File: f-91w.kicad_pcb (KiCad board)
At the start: 4 copper layers, 24.4 x 24.4 mm, 46 parts, among them P1 CONN_01X01, P10 CONN_01X01, P11 CONN_01X01, P13 CONN_01X01, P14 CONN_01X01, P2 CONN_01X01, P3 CONN_01X01, P5 CONN_01X01, P6 CONN_01X01, P7 CONN_01X01, P8 CONN_01X01, P9 CONN_01X01, Q1 BC846, U1 CY8C4248LQI-BL483, U2 LCD-F-91W, U3 BME680, Y1 32.768KHz, Y2 24MHz

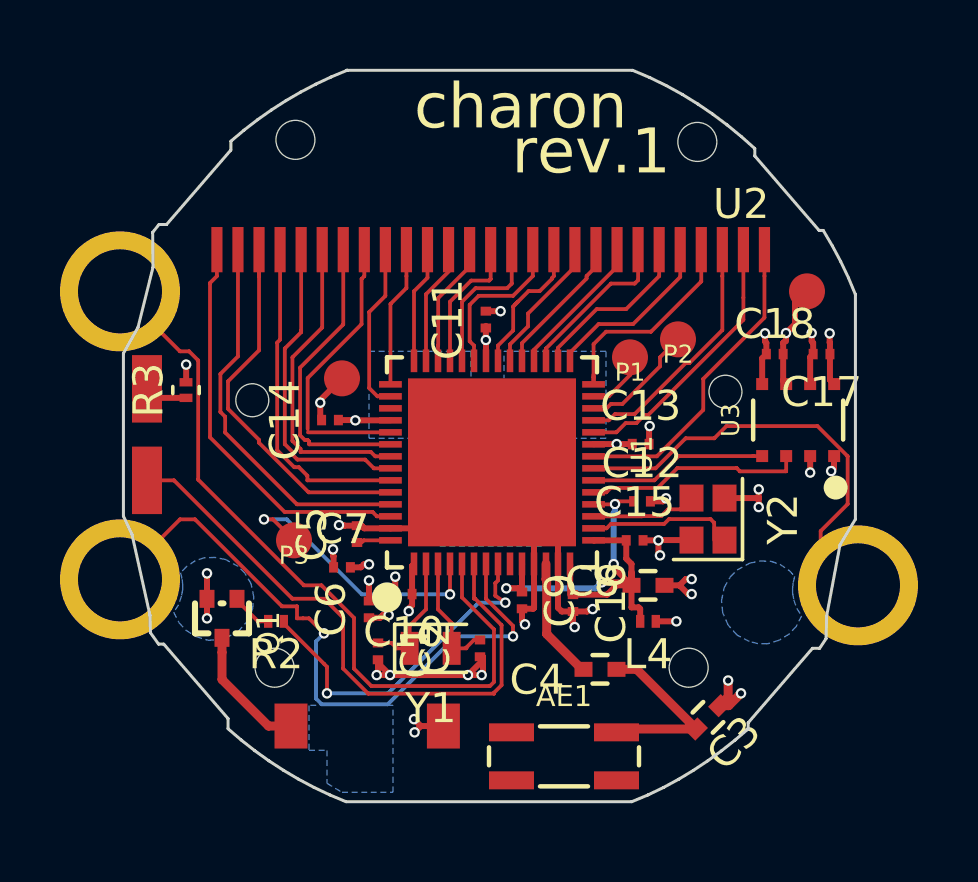
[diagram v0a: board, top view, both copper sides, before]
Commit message: Add outer ground planes, keepout and stitching vias for antenna
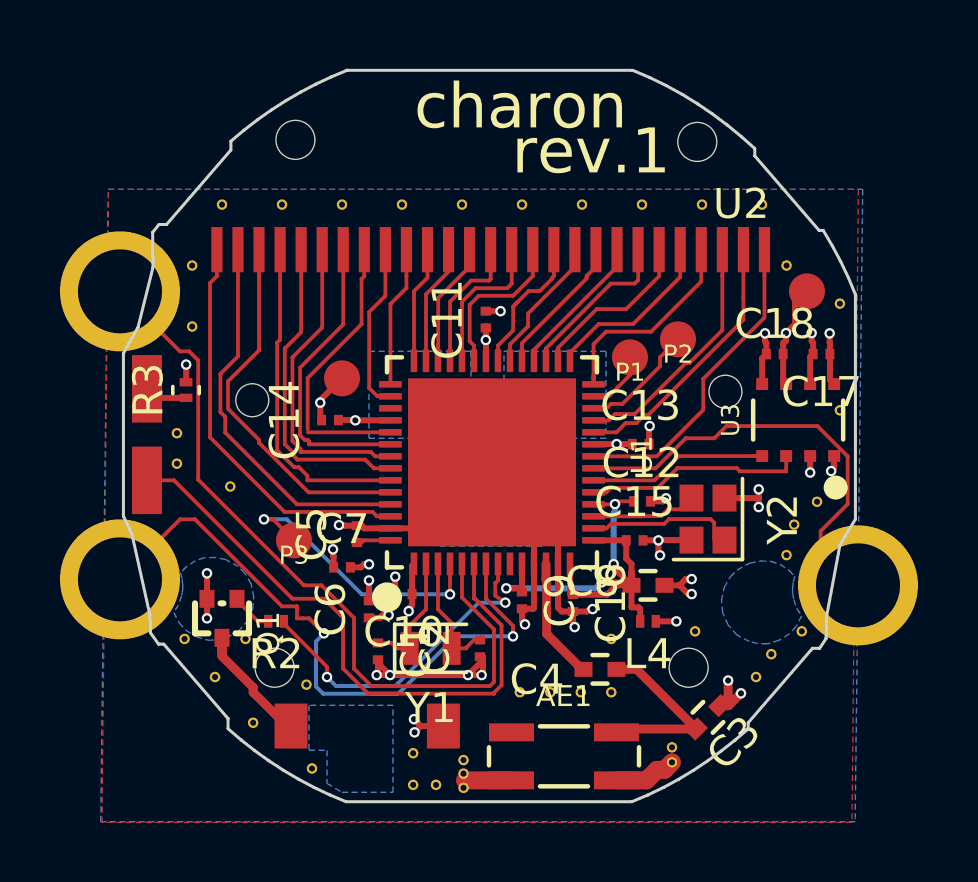
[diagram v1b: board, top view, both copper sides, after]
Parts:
- added REF**: STITCHING_VIA_0.2mm, f-91w:STITCHING_VIA_0.2mm, F.Cu at (67.0, 89.4)
- added REF**: STITCHING_VIA_0.2mm, f-91w:STITCHING_VIA_0.2mm, F.Cu at (49.0, 89.4)
- added REF**: STITCHING_VIA_0.2mm, f-91w:STITCHING_VIA_0.2mm, F.Cu at (69.6, 96.3)
- added REF**: STITCHING_VIA_0.2mm, f-91w:STITCHING_VIA_0.2mm, F.Cu at (67.8, 91.4)
- added REF**: STITCHING_VIA_0.2mm, f-91w:STITCHING_VIA_0.2mm, F.Cu at (69.6, 92.7)
- added REF**: STITCHING_VIA_0.2mm, f-91w:STITCHING_VIA_0.2mm, F.Cu at (48.0, 93.5)
- added REF**: STITCHING_VIA_0.2mm, f-91w:STITCHING_VIA_0.2mm, F.Cu at (48.0, 91.4)
- added REF**: STITCHING_VIA_0.2mm, f-91w:STITCHING_VIA_0.2mm, F.Cu at (48.8, 105.2)
- added REF**: STITCHING_VIA_0.2mm, f-91w:STITCHING_VIA_0.2mm, F.Cu at (47.8, 103.9)
- added REF**: STITCHING_VIA_0.2mm, f-91w:STITCHING_VIA_0.2mm, F.Cu at (50.0, 106.7)
- added REF**: STITCHING_VIA_0.2mm, f-91w:STITCHING_VIA_0.2mm, F.Cu at (51.8, 105.4)
- added REF**: STITCHING_VIA_0.2mm, f-91w:STITCHING_VIA_0.2mm, F.Cu at (65.0, 89.4)
- added REF**: STITCHING_VIA_0.2mm, f-91w:STITCHING_VIA_0.2mm, F.Cu at (68.8, 99.3)
- added REF**: STITCHING_VIA_0.2mm, f-91w:STITCHING_VIA_0.2mm, F.Cu at (66.8, 105.2)
- added REF**: STITCHING_VIA_0.2mm, f-91w:STITCHING_VIA_0.2mm, F.Cu at (55.4, 107.7)
- added REF**: STITCHING_VIA_0.2mm, f-91w:STITCHING_VIA_0.2mm, F.Cu at (64.0, 107.5)
- added REF**: STITCHING_VIA_0.2mm, f-91w:STITCHING_VIA_0.2mm, F.Cu at (64.0, 108.0)
- added REF**: STITCHING_VIA_0.2mm, f-91w:STITCHING_VIA_0.2mm, F.Cu at (52.0, 108.2)
- added REF**: STITCHING_VIA_0.2mm, f-91w:STITCHING_VIA_0.2mm, F.Cu at (57.0, 108.4)
- added REF**: STITCHING_VIA_0.2mm, f-91w:STITCHING_VIA_0.2mm, F.Cu at (56.1, 108.8)
- added REF**: STITCHING_VIA_0.2mm, f-91w:STITCHING_VIA_0.2mm, F.Cu at (64.8, 103.6)
- added REF**: STITCHING_VIA_0.2mm, f-91w:STITCHING_VIA_0.2mm, F.Cu at (62.0, 103.9)
- added REF**: STITCHING_VIA_0.2mm, f-91w:STITCHING_VIA_0.2mm, F.Cu at (63.0, 89.4)
- added REF**: STITCHING_VIA_0.2mm, f-91w:STITCHING_VIA_0.2mm, F.Cu at (47.5, 98.0)
- added REF**: STITCHING_VIA_0.2mm, f-91w:STITCHING_VIA_0.2mm, F.Cu at (47.5, 97.0)
- added REF**: STITCHING_VIA_0.2mm, f-91w:STITCHING_VIA_0.2mm, F.Cu at (49.3, 98.8)
- added REF**: STITCHING_VIA_0.2mm, f-91w:STITCHING_VIA_0.2mm, F.Cu at (68.1, 100.1)
- added REF**: STITCHING_VIA_0.2mm, f-91w:STITCHING_VIA_0.2mm, F.Cu at (67.3, 104.4)
- added REF**: STITCHING_VIA_0.2mm, f-91w:STITCHING_VIA_0.2mm, F.Cu at (67.8, 101.1)
- added REF**: STITCHING_VIA_0.2mm, f-91w:STITCHING_VIA_0.2mm, F.Cu at (68.3, 103.6)
- added REF**: STITCHING_VIA_0.2mm, f-91w:STITCHING_VIA_0.2mm, F.Cu at (49.8, 103.9)
- added REF**: STITCHING_VIA_0.2mm, f-91w:STITCHING_VIA_0.2mm, F.Cu at (62.0, 105.7)
- added REF**: STITCHING_VIA_0.2mm, f-91w:STITCHING_VIA_0.2mm, F.Cu at (61.0, 105.7)
- added REF**: STITCHING_VIA_0.2mm, f-91w:STITCHING_VIA_0.2mm, F.Cu at (61.0, 89.4)
- added REF**: STITCHING_VIA_0.2mm, f-91w:STITCHING_VIA_0.2mm, F.Cu at (59.9, 105.7)
- added REF**: STITCHING_VIA_0.2mm, f-91w:STITCHING_VIA_0.2mm, F.Cu at (58.9, 105.7)
- added REF**: STITCHING_VIA_0.2mm, f-91w:STITCHING_VIA_0.2mm, F.Cu at (57.0, 108.8)
- added REF**: STITCHING_VIA_0.2mm, f-91w:STITCHING_VIA_0.2mm, F.Cu at (57.0, 107.9)
- added REF**: STITCHING_VIA_0.2mm, f-91w:STITCHING_VIA_0.2mm, F.Cu at (59.0, 89.4)
- added REF**: STITCHING_VIA_0.2mm, f-91w:STITCHING_VIA_0.2mm, F.Cu at (55.4, 108.8)
- added REF**: STITCHING_VIA_0.2mm, f-91w:STITCHING_VIA_0.2mm, F.Cu at (57.0, 89.4)
- added REF**: STITCHING_VIA_0.2mm, f-91w:STITCHING_VIA_0.2mm, F.Cu at (55.0, 89.4)
- added REF**: STITCHING_VIA_0.2mm, f-91w:STITCHING_VIA_0.2mm, F.Cu at (53.0, 89.4)
- added REF**: STITCHING_VIA_0.2mm, f-91w:STITCHING_VIA_0.2mm, F.Cu at (51.0, 89.4)
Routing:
- net GND: track 44.0 -> 47.6 mm
- net /B_MODE: track 22.1 -> 21.6 mm
- net /BUZ_EN: track 11.8 -> 11.3 mm
- added copper zone on F.Cu, net GND

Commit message: Slightly increase stiching vias around antenna
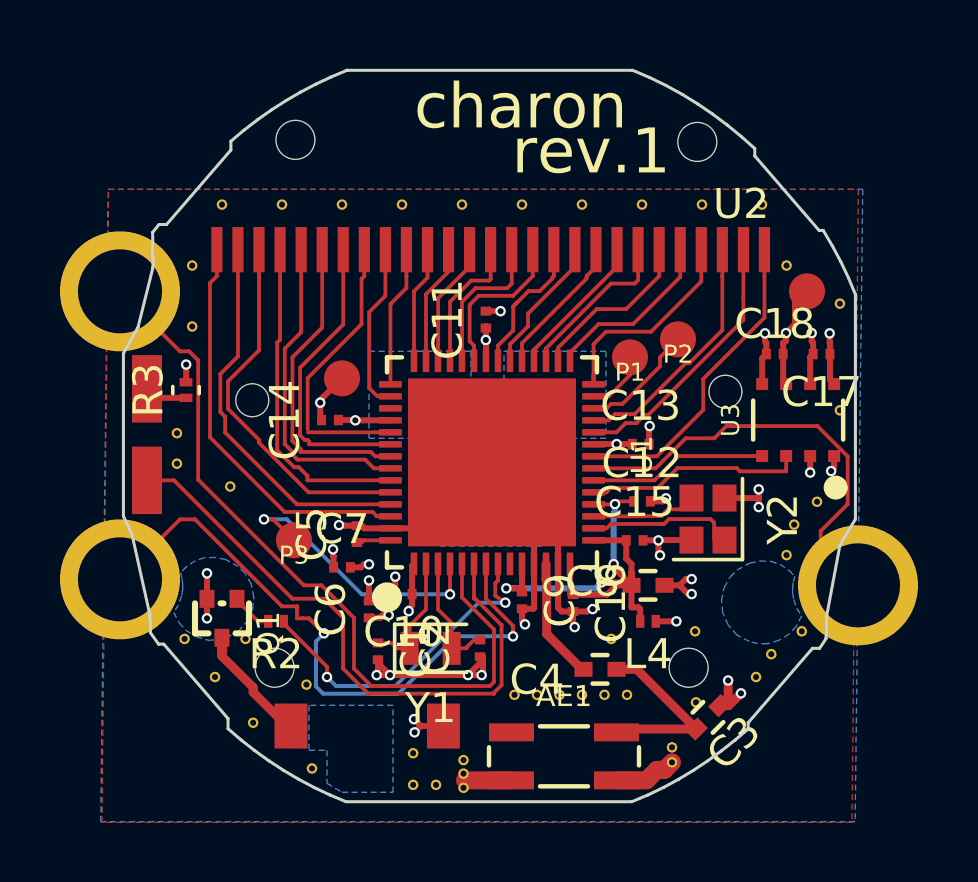
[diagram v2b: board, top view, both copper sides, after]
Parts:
- added REF**: STITCHING_VIA_0.2mm, f-91w:STITCHING_VIA_0.2mm, F.Cu at (64.8, 106.0)
- added REF**: STITCHING_VIA_0.2mm, f-91w:STITCHING_VIA_0.2mm, F.Cu at (62.5, 105.8)
- added REF**: STITCHING_VIA_0.2mm, f-91w:STITCHING_VIA_0.2mm, F.Cu at (61.8, 105.8)
- moved REF** 0.98 mm to (61.0, 105.8)
- moved REF** 0.72 mm to (60.2, 105.8)
- moved REF** 0.45 mm to (59.5, 105.8)
- moved REF** 0.20 mm to (58.8, 105.8)
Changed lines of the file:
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@@
     (tracks 529)
     (zones 0)
-    (modules 90)
+    (modules 93)
     (nets 51)
   )
@@
   )
   (module f-91w:STITCHING_VIA_0.2mm (layer F.Cu)
+    (at 64.8 106)
+    (fp_text reference REF** (at 0 1) (layer F.SilkS) hide
+      (effects (font (size 1 1) (thickness 0.15)))
+    )
+    (fp_text value STITCHING_VIA_0.2mm (at 0 -0.5) (layer F.Fab) hide
+      (effects (font (size 1 1) (thickness 0.15)))
+    )
+    (pad 1 thru_hole circle (at 0 0) (size 0.35 0.35) (drill 0.2) (layers *.Cu)
+      (net 2 GND) (zone_connect 2))
+  )
+  (module f-91w:STITCHING_VIA_0.2mm (layer F.Cu)
+    (at 62.5 105.75)
+    (fp_text reference REF** (at 0 1) (layer F.SilkS) hide
+      (effects (font (size 1 1) (thickness 0.15)))
+    )
+    (fp_text value STITCHING_VIA_0.2mm (at 0 -0.5) (layer F.Fab) hide
+      (effects (font (size 1 1) (thickness 0.15)))
+    )
+    (pad 1 thru_hole circle (at 0 0) (size 0.35 0.35) (drill 0.2) (layers *.Cu)
+      (net 2 GND) (zone_connect 2))
+  )
+  (module f-91w:STITCHING_VIA_0.2mm (layer F.Cu)
+    (at 61.75 105.75)
+    (fp_text reference REF** (at 0 1) (layer F.SilkS) hide
+      (effects (font (size 1 1) (thickness 0.15)))
+    )
+    (fp_text value STITCHING_VIA_0.2mm (at 0 -0.5) (layer F.Fab) hide
+      (effects (font (size 1 1) (thickness 0.15)))
+    )
+    (pad 1 thru_hole circle (at 0 0) (size 0.35 0.35) (drill 0.2) (layers *.Cu)
+      (net 2 GND) (zone_connect 2))
+  )
+  (module f-91w:STITCHING_VIA_0.2mm (layer F.Cu)
     (at 67 89.408)
     (fp_text reference REF** (at 0 1) (layer F.SilkS) hide
@@
   )
   (module f-91w:STITCHING_VIA_0.2mm (layer F.Cu)
-    (at 61.976 105.664)
-    (fp_text reference REF** (at 0 1) (layer F.SilkS) hide
-      (effects (font (size 1 1) (thickness 0.15)))
-    )
-    (fp_text value STITCHING_VIA_0.2mm (at 0 -0.5) (layer F.Fab) hide
-      (effects (font (size 1 1) (thickness 0.15)))
-    )
-    (pad 1 thru_hole circle (at 0 0) (size 0.35 0.35) (drill 0.2) (layers *.Cu)
-      (net 2 GND) (zone_connect 2))
-  )
-  (module f-91w:STITCHING_VIA_0.2mm (layer F.Cu)
-    (at 60.96 105.664)
-    (fp_text reference REF** (at 0 1) (layer F.SilkS) hide
-      (effects (font (size 1 1) (thickness 0.15)))
-    )
-    (fp_text value STITCHING_VIA_0.2mm (at 0 -0.5) (layer F.Fab) hide
-      (effects (font (size 1 1) (thickness 0.15)))
-    )
-    (pad 1 thru_hole circle (at 0 0) (size 0.35 0.35) (drill 0.2) (layers *.Cu)
-      (net 2 GND) (zone_connect 2))
-  )
-  (module f-91w:STITCHING_VIA_0.2mm (layer F.Cu)
-    (at 59.944 105.664)
-    (fp_text reference REF** (at 0 1) (layer F.SilkS) hide
-      (effects (font (size 1 1) (thickness 0.15)))
-    )
-    (fp_text value STITCHING_VIA_0.2mm (at 0 -0.5) (layer F.Fab) hide
-      (effects (font (size 1 1) (thickness 0.15)))
-    )
-    (pad 1 thru_hole circle (at 0 0) (size 0.35 0.35) (drill 0.2) (layers *.Cu)
-      (net 2 GND) (zone_connect 2))
-  )
-  (module f-91w:STITCHING_VIA_0.2mm (layer F.Cu)
-    (at 58.928 105.664)
-    (fp_text reference REF** (at 0 1) (layer F.SilkS) hide
-      (effects (font (size 1 1) (thickness 0.15)))
+    (at 61 105.75)
+    (fp_text reference REF** (at 0 1) (layer F.SilkS) hide
+      (effects (font (size 1 1) (thickness 0.15)))
+    )
+    (fp_text value STITCHING_VIA_0.2mm (at 0 -0.5) (layer F.Fab) hide
+      (effects (font (size 1 1) (thickness 0.15)))
+    )
+    (pad 1 thru_hole circle (at 0 0) (size 0.35 0.35) (drill 0.2) (layers *.Cu)
+      (net 2 GND) (zone_connect 2))
+  )
+  (module f-91w:STITCHING_VIA_0.2mm (layer F.Cu)
+    (at 60.25 105.75)
+    (fp_text reference REF** (at 0 1) (layer F.SilkS) hide
+      (effects (font (size 1 1) (thickness 0.15)))
+    )
+    (fp_text value STITCHING_VIA_0.2mm (at 0 -0.5) (layer F.Fab) hide
+      (effects (font (size 1 1) (thickness 0.15)))
+    )
+    (pad 1 thru_hole circle (at 0 0) (size 0.35 0.35) (drill 0.2) (layers *.Cu)
+      (net 2 GND) (zone_connect 2))
+  )
+  (module f-91w:STITCHING_VIA_0.2mm (layer F.Cu)
+    (at 59.5 105.75)
+    (fp_text reference REF** (at 0 1) (layer F.SilkS) hide
+      (effects (font (size 1 1) (thickness 0.15)))
+    )
+    (fp_text value STITCHING_VIA_0.2mm (at 0 -0.5) (layer F.Fab) hide
+      (effects (font (size 1 1) (thickness 0.15)))
+    )
+    (pad 1 thru_hole circle (at 0 0) (size 0.35 0.35) (drill 0.2) (layers *.Cu)
+      (net 2 GND) (zone_connect 2))
+  )
+  (module f-91w:STITCHING_VIA_0.2mm (layer F.Cu)
+    (at 58.75 105.75)
+    (fp_text reference REF** (at 0 1) (layer F.SilkS) hide
+      (effects (font (size 1 1) (thickness 0.15)))

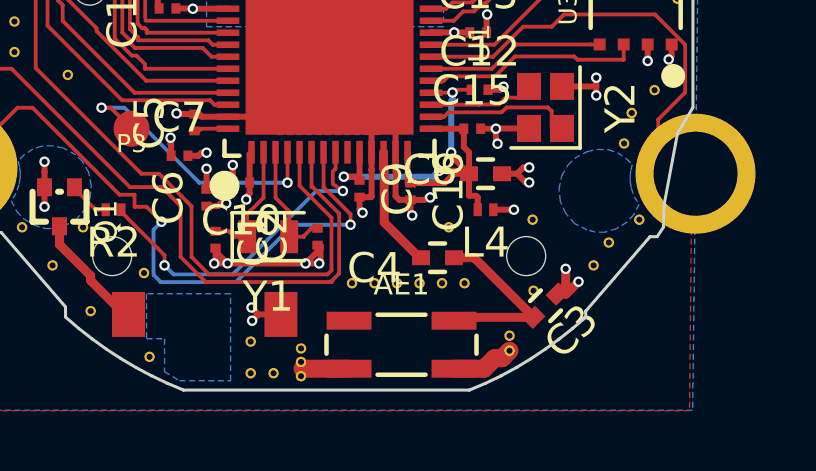
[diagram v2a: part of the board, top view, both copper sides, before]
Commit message: Update antenna footprint to add polarity markings
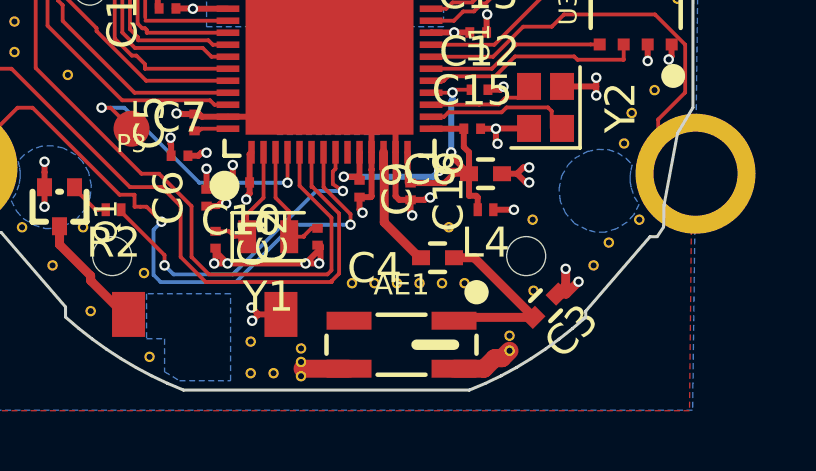
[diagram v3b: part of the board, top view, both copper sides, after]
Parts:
- AE1: value TBD -> 2450AT42E0100
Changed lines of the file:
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@@
 (kicad_pcb (version 4) (host pcbnew 4.0.7)
   (general
-    (links 0)
-    (no_connects 14)
+    (links 153)
+    (no_connects 1)
     (area 45.663181 84.883147 70.163247 109.362848)
     (thickness 0.6)
@@
     (35 F.Paste user)
     (36 B.SilkS user)
-    (37 F.SilkS user hide)
+    (37 F.SilkS user)
     (38 B.Mask user)
     (39 F.Mask user)
@@
     (pad "" np_thru_hole circle (at 0 0) (size 1.3 1.3) (drill 1.3) (layers *.Cu *.Mask))
   )
+  (module f-91w:TP_1.2mm (layer F.Cu)
+    (at 62.6 94.5)
+    (fp_text reference P1 (at 0 0.5) (layer F.SilkS)
+      (effects (font (size 0.6 0.6) (thickness 0.15)))
+    )
+    (fp_text value CONN_01X01 (at 0 -0.5) (layer F.Fab)
+      (effects (font (size 1 1) (thickness 0.15)))
+    )
+    (pad 1 smd circle (at 0 0) (size 1.2 1.2) (layers F.Cu F.Paste F.Mask)
+      (net 48 /SWCLK) (solder_mask_margin 0.07))
+  )
+  (module f-91w:TP_1.2mm (layer F.Cu)
+    (at 64.2 93.9)
+    (fp_text reference P2 (at 0 0.5) (layer F.SilkS)
+      (effects (font (size 0.6 0.6) (thickness 0.15)))
+    )
+    (fp_text value CONN_01X01 (at 0 -0.5) (layer F.Fab)
+      (effects (font (size 1 1) (thickness 0.15)))
+    )
+    (pad 1 smd circle (at 0 0) (size 1.2 1.2) (layers F.Cu F.Paste F.Mask)
+      (net 49 /SWDIO) (solder_mask_margin 0.07))
+  )
+  (module f-91w:TP_1.2mm (layer F.Cu)
+    (at 51.4 100.6)
+    (fp_text reference P3 (at 0 0.5) (layer F.SilkS)
+      (effects (font (size 0.6 0.6) (thickness 0.15)))
+    )
+    (fp_text value CONN_01X01 (at 0 -0.5) (layer F.Fab)
+      (effects (font (size 1 1) (thickness 0.15)))
+    )
+    (pad 1 smd circle (at 0 0) (size 1.2 1.2) (layers F.Cu F.Paste F.Mask)
+      (net 50 //XRES) (solder_mask_margin 0.07))
+  )
+  (module f-91w:STITCHING_VIA_0.2mm (layer F.Cu)
+    (at 55.372 108.75)
+    (fp_text reference REF** (at 0 1) (layer F.SilkS) hide
+      (effects (font (size 1 1) (thickness 0.15)))
+    )
+    (fp_text value STITCHING_VIA_0.2mm (at 0 -0.5) (layer F.Fab) hide
+      (effects (font (size 1 1) (thickness 0.15)))
+    )
+    (pad 1 thru_hole circle (at 0 0) (size 0.35 0.35) (drill 0.2) (layers *.Cu)
+      (net 2 GND) (zone_connect 2))
+  )
   (module f-91w:2450AT42E0100 (layer F.Cu)
     (at 60.4 107.8 180)
@@
       (effects (font (size 0.7 0.7) (thickness 0.15)))
     )
-    (fp_text value "TBD " (at 0 -1.5 180) (layer F.Fab)
+    (fp_text value 2450AT42E0100 (at 0 -1.5 180) (layer F.Fab)
       (effects (font (size 0.7 0.7) (thickness 0.1)))
     )
+    (fp_circle (center -2.5 1.75) (end -2.3 1.7) (layer F.SilkS) (width 0.4))
+    (fp_line (start -1.75 0) (end -0.5 0) (layer F.SilkS) (width 0.35))
     (fp_line (start -3.1 1.6) (end -3.1 -1.1) (layer F.CrtYd) (width 0.15))
     (fp_line (start 3.1 1.6) (end 3.1 -1.1) (layer F.CrtYd) (width 0.15))
@@
       (net 2 GND))
   )
-  (module f-91w:TP_1.2mm (layer F.Cu)
-    (at 62.6 94.5)
-    (fp_text reference P1 (at 0 0.5) (layer F.SilkS)
-      (effects (font (size 0.6 0.6) (thickness 0.15)))
-    )
-    (fp_text value CONN_01X01 (at 0 -0.5) (layer F.Fab)
-      (effects (font (size 1 1) (thickness 0.15)))
-    )
-    (pad 1 smd circle (at 0 0) (size 1.2 1.2) (layers F.Cu F.Paste F.Mask)
-      (net 48 /SWCLK) (solder_mask_margin 0.07))
-  )
-  (module f-91w:TP_1.2mm (layer F.Cu)
-    (at 64.2 93.9)
-    (fp_text reference P2 (at 0 0.5) (layer F.SilkS)
-      (effects (font (size 0.6 0.6) (thickness 0.15)))
-    )
-    (fp_text value CONN_01X01 (at 0 -0.5) (layer F.Fab)
-      (effects (font (size 1 1) (thickness 0.15)))
-    )
-    (pad 1 smd circle (at 0 0) (size 1.2 1.2) (layers F.Cu F.Paste F.Mask)
-      (net 49 /SWDIO) (solder_mask_margin 0.07))
-  )
-  (module f-91w:TP_1.2mm (layer F.Cu)
-    (at 51.4 100.6)
-    (fp_text reference P3 (at 0 0.5) (layer F.SilkS)
-      (effects (font (size 0.6 0.6) (thickness 0.15)))
-    )
-    (fp_text value CONN_01X01 (at 0 -0.5) (layer F.Fab)
-      (effects (font (size 1 1) (thickness 0.15)))
-    )
-    (pad 1 smd circle (at 0 0) (size 1.2 1.2) (layers F.Cu F.Paste F.Mask)
-      (net 50 //XRES) (solder_mask_margin 0.07))
-  )
-  (module f-91w:STITCHING_VIA_0.2mm (layer F.Cu)
-    (at 55.372 108.75)
-    (fp_text reference REF** (at 0 1) (layer F.SilkS) hide
-      (effects (font (size 1 1) (thickness 0.15)))
-    )
-    (fp_text value STITCHING_VIA_0.2mm (at 0 -0.5) (layer F.Fab) hide
-      (effects (font (size 1 1) (thickness 0.15)))
-    )
-    (pad 1 thru_hole circle (at 0 0) (size 0.35 0.35) (drill 0.2) (layers *.Cu)
-      (net 2 GND) (zone_connect 2))
-  )
   (gr_circle (center 53.84 106.79) (end 54.9 107.991) (layer Dwgs.User) (width 0.2))
